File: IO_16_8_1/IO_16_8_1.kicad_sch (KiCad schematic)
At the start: 77 parts, among them J1 Conn_01x06, J2 nmount JST 1mm QWIIC, J3 nmount SW Debug, J4 USB_C_Receptacle_USB2.0, J5 Conn_01x06, SW1 Reset, SW2 Boot, SW3 SW_DIP_x04, U1 ADM3483, U2 W25Q32JVSS, U3 RP2040, U4 LMV321, U5 SN74AHCT1G125, U6 AP2112K-3.3, Y1 12MHz,18pF

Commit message: routed
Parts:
- added TP2: TP_GND, Connector_Pin:Pin_D1.0mm_L10.0mm, symbol Connector:TestPoint
- SW3: value SW_DIP_x04 -> ADDRESS
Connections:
- net GND: now also TP2.1
- net SHD: now reaches C1.1, J1.3 (Pin_3), R2.1
- net A: now reaches D1.1 (K), J1.1 (Pin_1), R3.2, R4.1, U1.6 (A)
- net B: now reaches D2.1 (K), J1.2 (Pin_2), R4.2, R5.1, U1.7 (B)
- net LED_Strip renamed Out_S
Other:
- note added: "25"
- note added: "Terminal nr."
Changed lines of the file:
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@@
     (stroke (width 0) (type default) (color 0 0 0 0))
   )
+  (wire (pts (xy 284.48 160.02) (xy 284.48 171.45))
+    (stroke (width 0) (type default) (color 0 0 0 0))
+  )
   (wire (pts (xy 363.22 102.87) (xy 363.22 105.41))
     (stroke (width 0) (type default) (color 0 0 0 0))
@@
     (effects (font (size 1.27 1.27)) (justify left bottom))
   )
+  (text "Terminal nr." (at 378.46 109.22 0)
+    (effects (font (size 1.27 1.27)) (justify left bottom))
+  )
+  (text "25" (at 372.11 110.49 0)
+    (effects (font (size 3 3) (thickness 0.6) bold) (justify left bottom))
+  )
   (text "PPUC" (at 316.23 265.43 0)
     (effects (font (size 5 5) bold) (justify left bottom))
@@
     (effects (font (size 1.27 1.27)) (justify left bottom))
   )
+  (label "B" (at 39.37 57.15 0)
+    (effects (font (size 1.27 1.27)) (justify left bottom))
+  )
   (label "Out_1" (at 323.85 208.28 180)
     (effects (font (size 1.27 1.27)) (justify right bottom))
@@
     (effects (font (size 1.27 1.27)) (justify left bottom))
   )
+  (label "SHD" (at 39.37 59.69 0)
+    (effects (font (size 1.27 1.27)) (justify left bottom))
+  )
   (label "In_11" (at 99.06 232.41 0)
     (effects (font (size 1.27 1.27)) (justify left bottom))
@@
     (effects (font (size 1.27 1.27)) (justify left bottom))
   )
-  (label "LED_Strip" (at 327.66 107.95 0)
+  (label "Out_S" (at 327.66 107.95 0)
     (effects (font (size 1.27 1.27)) (justify left bottom))
   )
@@
     (effects (font (size 1.27 1.27)) (justify left bottom))
   )
+  (label "A" (at 39.37 54.61 0)
+    (effects (font (size 1.27 1.27)) (justify left bottom))
+  )
   (label "Q_SCLK" (at 105.41 124.46 0)
     (effects (font (size 1.27 1.27)) (justify left bottom))
@@
     (in_bom yes) (on_board yes) (fields_autoplaced)
     (property "Reference" "SW3" (id 0) (at 250.19 201.93 0))
-    (property "Value" "SW_DIP_x04" (id 1) (at 250.19 204.47 0))
+    (property "Value" "ADDRESS" (id 1) (at 250.19 204.47 0))
     (property "Footprint" "Button_Switch_SMD:SW_DIP_SPSTx04_Slide_6.7x11.72mm_W8.61mm_P2.54mm_LowProfile" (id 2) (at 250.19 214.63 0)
       (effects (font (size 1.27 1.27)) hide)
@@
     (pin "2")
   )
+  (symbol (lib_id "Connector:TestPoint") (at 284.48 160.02 0) (unit 1)
+    (in_bom yes) (on_board yes) (fields_autoplaced)
+    (property "Reference" "TP2" (id 0) (at 287.02 155.4479 0)
+      (effects (font (size 1.27 1.27)) (justify left))
+    )
+    (property "Value" "TP_GND" (id 1) (at 287.02 157.9879 0)
+      (effects (font (size 1.27 1.27)) (justify left))
+    )
+    (property "Footprint" "Connector_Pin:Pin_D1.0mm_L10.0mm" (id 2) (at 289.56 160.02 0)
+      (effects (font (size 1.27 1.27)) hide)
+    )
+    (property "Datasheet" "~" (id 3) (at 289.56 160.02 0)
+      (effects (font (size 1.27 1.27)) hide)
+    )
+    (pin "1")
+  )
   (symbol (lib_id "Memory_Flash:W25Q32JVSS") (at 127 121.92 0) (unit 1)
     (in_bom yes) (on_board yes) (fields_autoplaced)
@@
     (pin "1")
   )
+  (symbol (lib_id "power:GND") (at 284.48 171.45 0) (unit 1)
+    (in_bom yes) (on_board yes)
+    (property "Reference" "#PWR05" (id 0) (at 284.48 177.8 0)
+      (effects (font (size 1.27 1.27)) hide)
+    )
+    (property "Value" "GND" (id 1) (at 284.607 175.8442 0))
+    (property "Footprint" "" (id 2) (at 284.48 171.45 0)
+      (effects (font (size 1.27 1.27)) hide)
+    )
+    (property "Datasheet" "" (id 3) (at 284.48 171.45 0)
+      (effects (font (size 1.27 1.27)) hide)
+    )
+    (pin "1")
+  )
   (symbol (lib_id "power:GND") (at 182.88 227.33 0) (unit 1)
     (in_bom yes) (on_board yes)
@@
   (symbol (lib_id "Connector_Generic:Conn_01x06") (at 370.84 102.87 0) (unit 1)
     (in_bom yes) (on_board yes)
-    (property "Reference" "J5" (id 0) (at 372.872 103.0732 0)
+    (property "Reference" "J5" (id 0) (at 373.38 99.06 0)
       (effects (font (size 1.27 1.27)) (justify left))
     )
-    (property "Value" "Conn_01x06" (id 1) (at 372.872 105.3846 0)
+    (property "Value" "Conn_01x06" (id 1) (at 373.38 101.6 0)
       (effects (font (size 1.27 1.27)) (justify left))
     )
@@
       (reference "#PWR04") (unit 1) (value "+3V3") (footprint "")
     )
+    (path "/e3017a0d-2b64-4cff-bd61-8ea5f6de0917"
+      (reference "#PWR05") (unit 1) (value "GND") (footprint "")
+    )
     (path "/cd816392-78de-4c49-bac0-ed4e8ab59e24"
       (reference "#PWR0101") (unit 1) (value "GND") (footprint "")
@@
     )
     (path "/6aa10f17-6588-457f-8d73-2d1fd3a7d131"
-      (reference "SW3") (unit 1) (value "SW_DIP_x04") (footprint "Button_Switch_SMD:SW_DIP_SPSTx04_Slide_6.7x11.72mm_W8.61mm_P2.54mm_LowProfile")
+      (reference "SW3") (unit 1) (value "ADDRESS") (footprint "Button_Switch_SMD:SW_DIP_SPSTx04_Slide_6.7x11.72mm_W8.61mm_P2.54mm_LowProfile")
     )
     (path "/7102ec04-e14a-4514-8577-c54824d6a045"
       (reference "TP1") (unit 1) (value "TP_LED") (footprint "Connector_Pin:Pin_D1.0mm_L10.0mm")
     )
+    (path "/d417f957-d5cb-4eac-918f-cc66a74ba75c"
+      (reference "TP2") (unit 1) (value "TP_GND") (footprint "Connector_Pin:Pin_D1.0mm_L10.0mm")
+    )
     (path "/ee82bca5-2167-414e-9dea-68323baf03fe"

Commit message: v010
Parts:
- U2: value W25Q32JVSS -> W25Q128JVSIQ
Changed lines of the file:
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@@
       (effects (font (size 1.27 1.27)) (justify left))
     )
-    (property "Value" "W25Q32JVSS" (id 1) (at 129.0194 111.76 0)
+    (property "Value" "W25Q128JVSIQ" (id 1) (at 129.0194 111.76 0)
       (effects (font (size 1.27 1.27)) (justify left))
     )
@@
       (effects (font (size 1.27 1.27)) hide)
     )
-    (property "Datasheet" "http://www.winbond.com/resource-files/w25q32jv%20revg%2003272018%20plus.pdf" (id 3) (at 127 121.92 0)
+    (property "Datasheet" "" (id 3) (at 127 121.92 0)
       (effects (font (size 1.27 1.27)) hide)
     )
@@
     )
     (path "/d8a3cc26-5476-4935-9578-7934c177bfd0"
-      (reference "U2") (unit 1) (value "W25Q32JVSS") (footprint "Package_SO:SOIC-8_5.23x5.23mm_P1.27mm")
+      (reference "U2") (unit 1) (value "W25Q128JVSIQ") (footprint "Package_SO:SOIC-8_5.23x5.23mm_P1.27mm")
     )
     (path "/f8f68e11-9cec-4282-b57d-6f23ac1839ad"

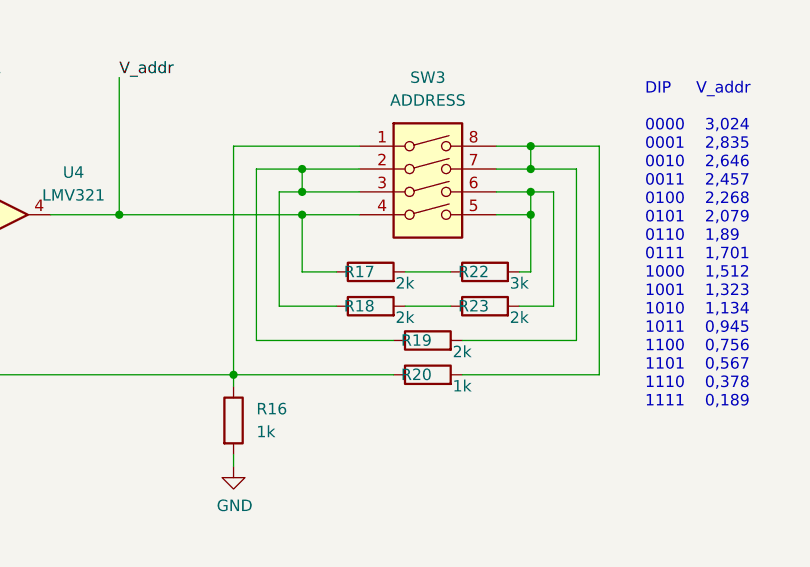
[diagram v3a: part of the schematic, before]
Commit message: changed R17
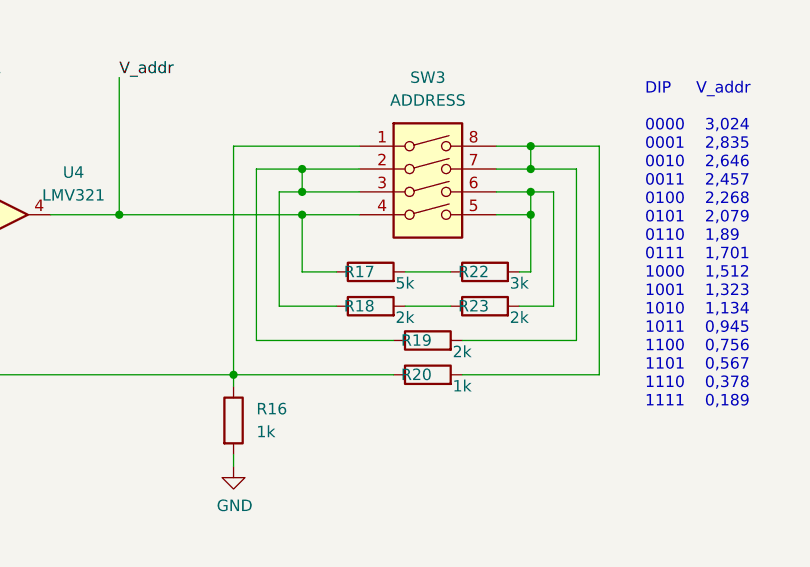
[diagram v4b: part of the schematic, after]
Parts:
- R17: value 2k -> 5k
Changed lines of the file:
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@@
     (in_bom yes) (on_board yes)
     (property "Reference" "R17" (id 0) (at 242.57 223.52 90))
-    (property "Value" "2k" (id 1) (at 247.65 224.79 90))
+    (property "Value" "5k" (id 1) (at 247.65 224.79 90))
     (property "Footprint" "Resistor_SMD:R_0603_1608Metric" (id 2) (at 243.84 225.298 90)
       (effects (font (size 1.27 1.27)) hide)
@@
     )
     (path "/9d1a26ac-4cd3-4cd7-b134-15cca7759d09"
-      (reference "R17") (unit 1) (value "2k") (footprint "Resistor_SMD:R_0603_1608Metric")
+      (reference "R17") (unit 1) (value "5k") (footprint "Resistor_SMD:R_0603_1608Metric")
     )
     (path "/135913b1-40cb-4f29-858e-e340673c9948"
